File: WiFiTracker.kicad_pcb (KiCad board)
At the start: 2 copper layers, 56.4 x 56.4 mm, 33 parts, among them IC1 CP2104, P1 Battery, P2 USB_B, Q1 MMBT2222A, Q2 MMBT2222A, SW1 SW_RESET, U1 RFM95W-868S2, U2 AP2114, U3 MCP73831T-2ATI/OT, U4 ESP8266-12E

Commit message: Check PCB V0.1
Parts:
- removed P1: Battery, Pin_Headers:Pin_Header_Angled_1x02_Pitch2.54mm
- removed R3: 10K, Resistors_SMD:R_0805_HandSoldering
- added ANT: ANT, Connect:1pin, F.Cu at (142.7, 110.9)
- added G***: LOGO, TIH:electronic_cats_logo_4x3, F.Cu at (143.5, 103.2)
- added P3: USB_B, Connectors_Molex:USB_Micro-B_Molex_47346-0001, B.Cu at (119.5, 105.5)
- added REF***: OSHW-Logo2_9.8x8mm_SilkScreen, Symbols:OSHW-Logo2_9.8x8mm_SilkScreen, B.Cu at (130.1, 86.2)
- C4, R1, R11, R13, R2: moved to B.Cu
- P2: value USB_B -> Battery; footprint Connectors_Molex:USB_Micro-B_Molex_47346-0001 -> Pin_Headers:Pin_Header_Angled_1x02_Pitch2.54mm; moved to B.Cu
- R4, R8: value 100K -> 10K
- R7: value 100K -> 330R
- R9: value 330R -> 10K; moved to B.Cu
- U1: footprint TIH:XCVR_RFM95W-868S2 -> rfm95:XCVR_RFM95W-868S2; moved to B.Cu
- U3: moved to F.Cu
- moved R13 48.9 mm to (150.8, 86.2), turned to 270 degrees
- moved R11 42.1 mm to (146.0, 86.0), turned to 270 degrees
- moved R5 42.1 mm to (150.5, 108.0), turned to 270 degrees
- moved U2 39.0 mm to (144.7, 103.0)
- moved U4 37.9 mm to (155.6, 78.7), turned to 270 degrees
- moved R1 37.5 mm to (133.0, 78.3), turned to 270 degrees
- moved DONE 34.5 mm to (130.0, 78.0), turned to 270 degrees
- moved Q2 34.4 mm to (152.2, 112.2), turned to 90 degrees
- moved R4 33.0 mm to (134.5, 82.9), turned to 90 degrees
- moved R10 32.3 mm to (142.5, 97.2), turned to 180 degrees
- moved R2 31.3 mm to (136.1, 78.3), turned to 270 degrees
- moved C2 31.1 mm to (132.0, 83.0), turned to 90 degrees
- moved C4 31.1 mm to (136.3, 92.8), turned to 90 degrees
- moved IC1 29.1 mm to (130.5, 105.0)
- moved C3 27.5 mm to (129.5, 92.6), turned to 270 degrees
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- renumbered D3 to CHG, D4 to DONE, SW1 to RESET
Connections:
- P2 pad 1: VCC -> +BATT
- P2 pad 2: Net-(IC1-Pad4) -> GND
- R10 pad 1: +3V3 -> /GPIO15
- R10 pad 2: /RST -> GND
- R11 pad 2: /CH_PD -> /GPIO2
- R4 pad 1: /ADC -> Net-(R4-Pad1)
- R7 pad 1: Net-(R7-Pad1) -> /GPIO0
- R7 pad 2: /ADC -> Net-(D5-Pad1)
- R8 pad 1: /A0 -> +3V3
- R8 pad 2: Net-(R7-Pad1) -> /RST
- R9 pad 1: /GPIO0 -> +3V3
- R9 pad 2: Net-(D5-Pad1) -> /CH_PD
- U1 pad 5: /GPIO15 -> /GPIO16
- U2 pad 3: Net-(R14-Pad1) -> Net-(U2-Pad3)
- U3 pad 5: Net-(R3-Pad1) -> Net-(R4-Pad1)
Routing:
- net GND: track 0.00 -> 128.2 mm, vias 0 -> 9
- net +3V3: track 0.00 -> 102.7 mm, vias 0 -> 6
- net /DTR: track 0.00 -> 63.6 mm, vias 0 -> 2
- net VCC: track 0.00 -> 47.6 mm, vias 0 -> 5
- net /RESET: track 0.00 -> 44.6 mm, vias 0 -> 2
- net Net-(C1-Pad1): track 0.00 -> 41.2 mm, vias 0 -> 3
- net /GPIO13: track 0.00 -> 33.8 mm, vias 0 -> 1
- net /TXD: track 0.00 -> 33.3 mm, vias 0 -> 2
- net /RXD: track 0.00 -> 33.2 mm, vias 0 -> 1
- net Net-(R1-Pad1): track 0.00 -> 31.7 mm, vias 0 -> 1
- net /RST: track 0.00 -> 29.6 mm, vias 0 -> 2
- net +BATT: track 0.00 -> 24.2 mm
- net /GPIO15: track 0.00 -> 21.4 mm, vias 0 -> 2
- net Net-(R4-Pad1): track 0.00 -> 17.4 mm, vias 0 -> 4
- net /GPIO0: track 0.00 -> 13.0 mm
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- added copper zone on B.Cu, net GND
- added copper zone on F.Cu, net GND
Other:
- board size 56.4 x 56.4 mm -> 40.6 x 39.6 mm
- net class Default: trace_width 0.25 -> 0.3; via_drill 0.4 -> 0.5
- net class VCC added: clearance 0.2, trace_width 0.5, via_dia 0.6, via_drill 0.4
- rule trace_min: 0.2 -> 0.25

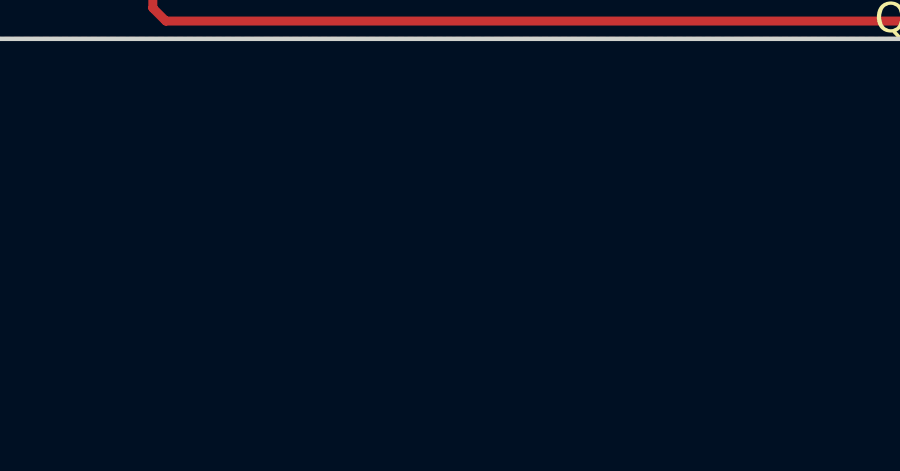
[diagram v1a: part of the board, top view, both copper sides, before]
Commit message: Added Lib AP2114
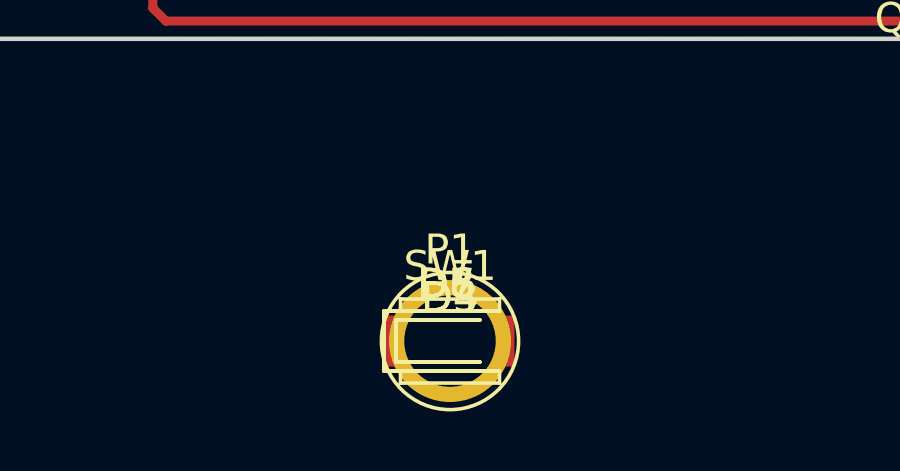
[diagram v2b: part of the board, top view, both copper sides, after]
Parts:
- added D3: CHG, LEDs:LED_0805, F.Cu at (137.1, 125.3)
- added D4: DONE, LEDs:LED_0805, F.Cu at (137.1, 125.3)
- added D6, D7, D8: D, Diodes_SMD:D_SOD-123F, F.Cu at (137.1, 125.3)
- added P1: ANT, Connect:1pin, F.Cu at (137.1, 125.3)
- added SW1: SW_RESET, Buttons_Switches_SMD:SW_SPST_B3U-1000P, F.Cu at (137.1, 125.3)
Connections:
- net /SDA renamed /GPIO4
- U1 pad 14: Net-(U1-Pad14) -> /DIO0
- U1 pad 15: Net-(U1-Pad15) -> /DIO1
- U1 pad 16: Net-(U1-Pad16) -> /DIO2
- U1 pad 5: /GPIO16 -> /GPIO5
- U2 pad 1: Net-(C1-Pad1) -> GND
- U2 pad 2: GND -> +3V3
- U2 pad 3: Net-(U2-Pad3) -> Net-(C1-Pad1)
- U4 pad 20: /SCL -> /GPIO5
- U4 pad 4: /RST_RN -> /RESET
- U4 pad 5: /STX -> /GPIO14
- U4 pad 6: /SRX -> /GPIO12
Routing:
- net Net-(C1-Pad1): track 41.2 -> 17.7 mm, vias 3 -> 2
- net GND: track 128.2 -> 139.9 mm, vias 9 -> 10
- net +3V3: track 102.7 -> 114.4 mm

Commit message: Arreglados los pines, se mamaron
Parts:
- removed D3: CHG, LEDs:LED_0805
- removed D4: DONE, LEDs:LED_0805
- removed P1: ANT, Connect:1pin
- removed SW1: SW_RESET, Buttons_Switches_SMD:SW_SPST_B3U-1000P
- C4: moved to F.Cu
- moved D7 23.3 mm to (121.8, 107.7)
- moved D8 21.5 mm to (121.8, 110.2)
- moved D6 19.8 mm to (121.8, 112.6)
- moved C4 0.13 mm to (136.4, 92.7), turned to 270 degrees
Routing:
- net /GPIO15: track 21.4 -> 77.6 mm, vias 2 -> 4
- net /GPIO12: track 0.00 -> 49.9 mm, vias 0 -> 3
- net /GPIO14: track 0.00 -> 45.5 mm, vias 0 -> 2
- net GND: track 139.9 -> 108.1 mm
- net /GPIO5: track 0.00 -> 24.5 mm
- net Net-(C1-Pad1): track 17.7 -> 36.8 mm, vias 2 -> 3
- net VCC: track 47.6 -> 59.3 mm
- net /RESET: track 44.6 -> 52.4 mm
- net /DIO0: track 0.00 -> 7.26 mm, vias 0 -> 1
- net /DIO1: track 0.00 -> 4.51 mm, vias 0 -> 1
- net /DIO2: track 0.00 -> 3.31 mm, vias 0 -> 1
- net +3V3: track 114.4 -> 111.5 mm
- net /DTR: track 63.6 -> 66.3 mm
- net +BATT: track 24.2 -> 26.2 mm
- net /RST: track 29.6 -> 31.2 mm
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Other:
- net class Default: via_drill 0.5 -> 0.3
- net class VCC: via_drill 0.4 -> 0.3

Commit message: Fix Reset connection
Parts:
- added D3: CHG, LEDs:LED_0805, F.Cu at (137.1, 125.3)
- added D4: DONE, LEDs:LED_0805, F.Cu at (137.1, 125.3)
- added P1: ANT, Connect:1pin, F.Cu at (137.1, 125.3)
- added SW1: SW_RESET, Buttons_Switches_SMD:SW_SPST_B3U-1000P, F.Cu at (137.1, 125.3)
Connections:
- IC1 pad 19: /RST -> /RTS
- R8 pad 2: /RST -> /RESET
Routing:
- net /RST: track 31.2 -> 4.64 mm, vias 2 -> 0
- net /RTS: track 3.34 -> 22.1 mm, vias 0 -> 2
- net /RESET: track 52.4 -> 60.3 mm
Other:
- board text added: "LoRaCatPet"
